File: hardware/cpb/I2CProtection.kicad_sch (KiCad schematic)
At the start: 16 parts, among them Q16 MBT2222ADW1T1, Q17 MBT2222ADW1T1, Q18 BSS138PS,115, Q19 BSS138PS,115

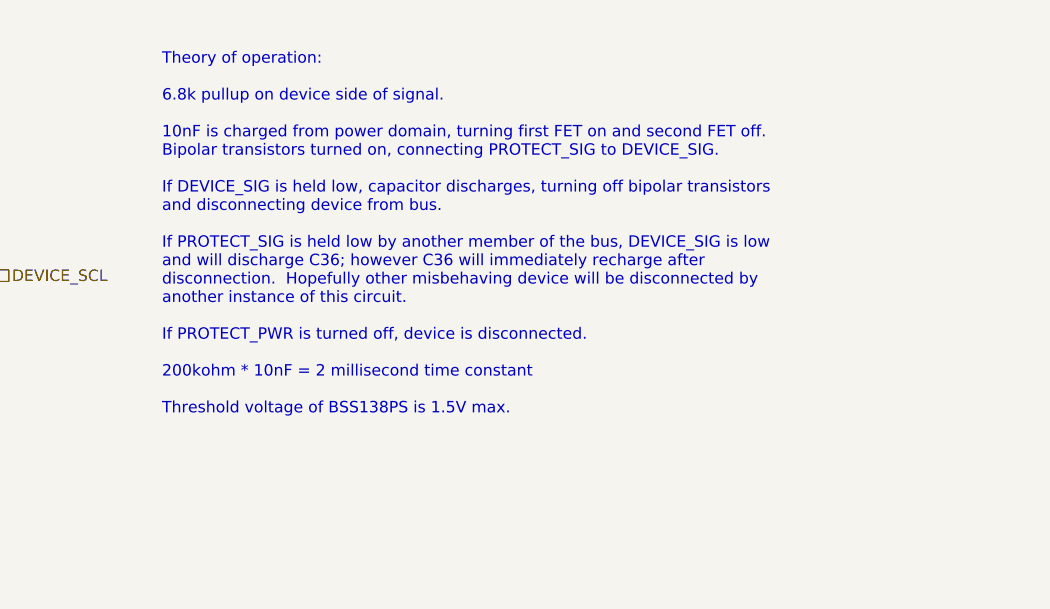
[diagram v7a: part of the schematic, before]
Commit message: hardware/cpb: changed labels, spread out components
changed vm labels, spread out somponents on Four Full Bridges sch;
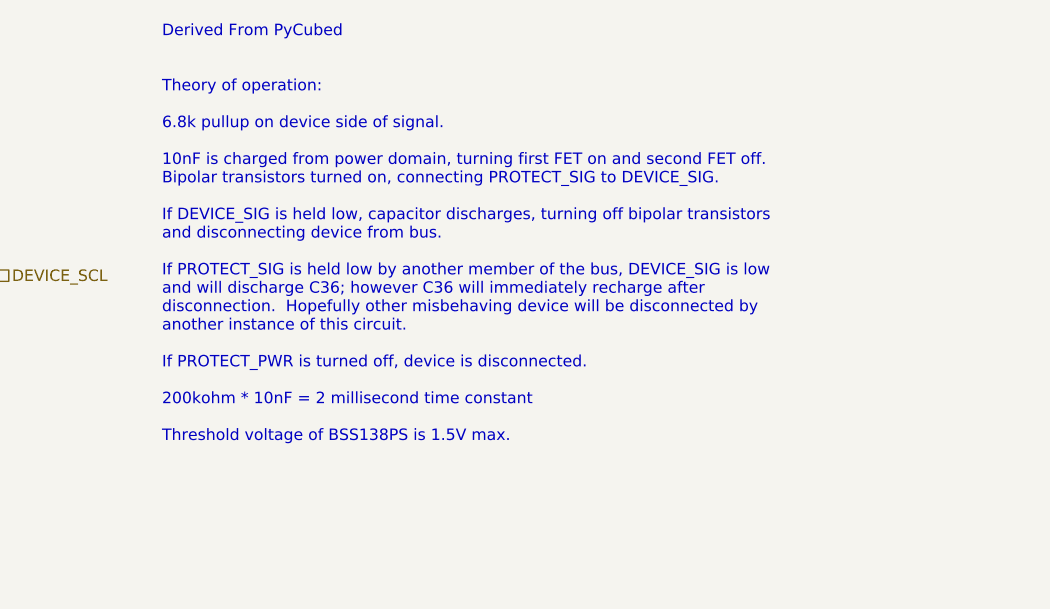
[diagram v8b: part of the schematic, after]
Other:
- note added: "Derived From PyCubed Theory of operation: 6.8k pullup on device side of signal. 10nF is charged from power domain, turning first FET on and second FET off. Bipolar transistors turned on, connecting PROTECT_SIG to DEVICE_SIG. If DEVICE_SIG is held low, capacitor discharges, turning off bipolar transistors and disconnecting device from bus. If PROTECT_SIG is held low by another member of the bus, D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"
- note removed: "Theory of operation: 6.8k pullup on device side of signal. 10nF is charged from power domain, turning first FET on and second FET off. Bipolar transistors turned on, connecting PROTECT_SIG to DEVICE_SIG. If DEVICE_SIG is held low, capacitor discharges, turning off bipolar transistors and disconnecting device from bus. If PROTECT_SIG is held low by another member of the bus, DEVICE_SIG is low and 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"
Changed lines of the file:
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@@
 		)
 	)
-	(text "Theory of operation:\n\n6.8k pullup on device side of signal.\n\n10nF is charged from power domain, turning first FET on and second FET off.\nBipolar transistors turned on, connecting PROTECT_SIG to DEVICE_SIG.\n\nIf DEVICE_SIG is held low, capacitor discharges, turning off bipolar transistors\nand disconnecting device from bus.\n\nIf PROTECT_SIG is held low by another member of the bus, DEVICE_SIG is low\nand will discharge C36; however C36 will immediately recharge after\ndisconnection.  Hopefully other misbehaving device will be disconnected by\nanother instance of this circuit.\n\nIf PROTECT_PWR is turned off, device is disconnected.\n\n200kohm * 10nF = 2 millisecond time constant\n\nThreshold voltage of BSS138PS is 1.5V max."
+	(text "Derived From PyCubed\n\n\nTheory of operation:\n\n6.8k pullup on device side of signal.\n\n10nF is charged from power domain, turning first FET on and second FET off.\nBipolar transistors turned on, connecting PROTECT_SIG to DEVICE_SIG.\n\nIf DEVICE_SIG is held low, capacitor discharges, turning off bipolar transistors\nand disconnecting device from bus.\n\nIf PROTECT_SIG is held low by another member of the bus, DEVICE_SIG is low\nand will discharge C36; however C36 will immediately recharge after\ndisconnection.  Hopefully other misbehaving device will be disconnected by\nanother instance of this circuit.\n\nIf PROTECT_PWR is turned off, device is disconnected.\n\n200kohm * 10nF = 2 millisecond time constant\n\nThreshold voltage of BSS138PS is 1.5V max."
 		(exclude_from_sim no)
 		(at 185.928 44.958 0)
